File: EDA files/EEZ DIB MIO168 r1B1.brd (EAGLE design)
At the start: 146 x 95 mm, 296 parts, among them IC1 M24C32-WMN6P, IC10 DAC7760IPWPR, IC11 DAC7760IPWPR, IC12 OPA376AIDBVR, IC13 DAC7563TDGSR, IC14 OPA2196IDR, IC15 BTS3408G, IC16 BTS3408G, IC17 BTS3408G, IC18 BTS3408G, IC19 74HC126PW,118, IC2 Si8641BB-B-IS1, IC20 TL431B, IC21 DG468DV-T1-E3, IC22 DG468DV-T1-E3, IC23 DG468DV-T1-E3, IC24 DG468DV-T1-E3, IC25 DG468DV-T1-E3, IC26 DG468DV-T1-E3, IC27 DG468DV-T1-E3, IC28 DG468DV-T1-E3, IC29 DG468DV-T1-E3, IC3 Si8641BB-B-IS1, IC30 DG468DV-T1-E3, IC31 DG468DV-T1-E3, IC32 DG468DV-T1-E3, IC33 DG468DV-T1-E3, IC34 DG468DV-T1-E3, IC35 OPA376AIDBVR, IC36 ADS8674IDBT, IC4 L78L12, IC5 LP2985-50DBVR, IC6 LP2985-33DBVR, IC7 L79L12, IC8 STM32F446ZCT6, IC9 OPA2196IDR, J1 4907, J2 503398-1892, Q1 2N7002PS, Q10 BSS169, Q11 BSS169, Q12 BSS169, Q13 BSS169, Q2 2N7002PS, Q3 2N7002PS, Q4 2N7002PS, Q5 2N7002PS, Q6 BSS169, Q7 BSS169, Q8 BSS169, Q9 BSS169, X1 77317-104-28LF, X2 SSW-106-02-S-S, X3 691327310016, X4 691327310016, Y1 25MHz

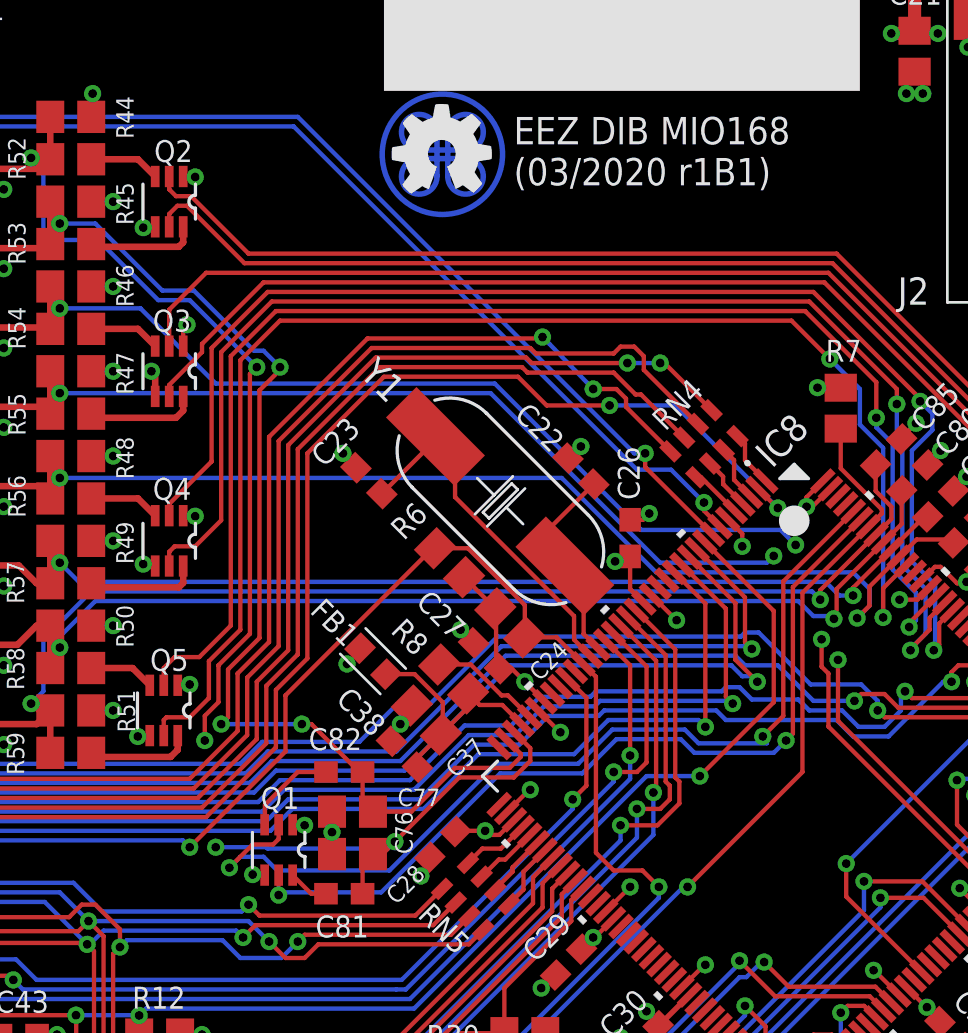
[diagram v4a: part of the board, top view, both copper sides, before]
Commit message: 2N7002PS package fixed
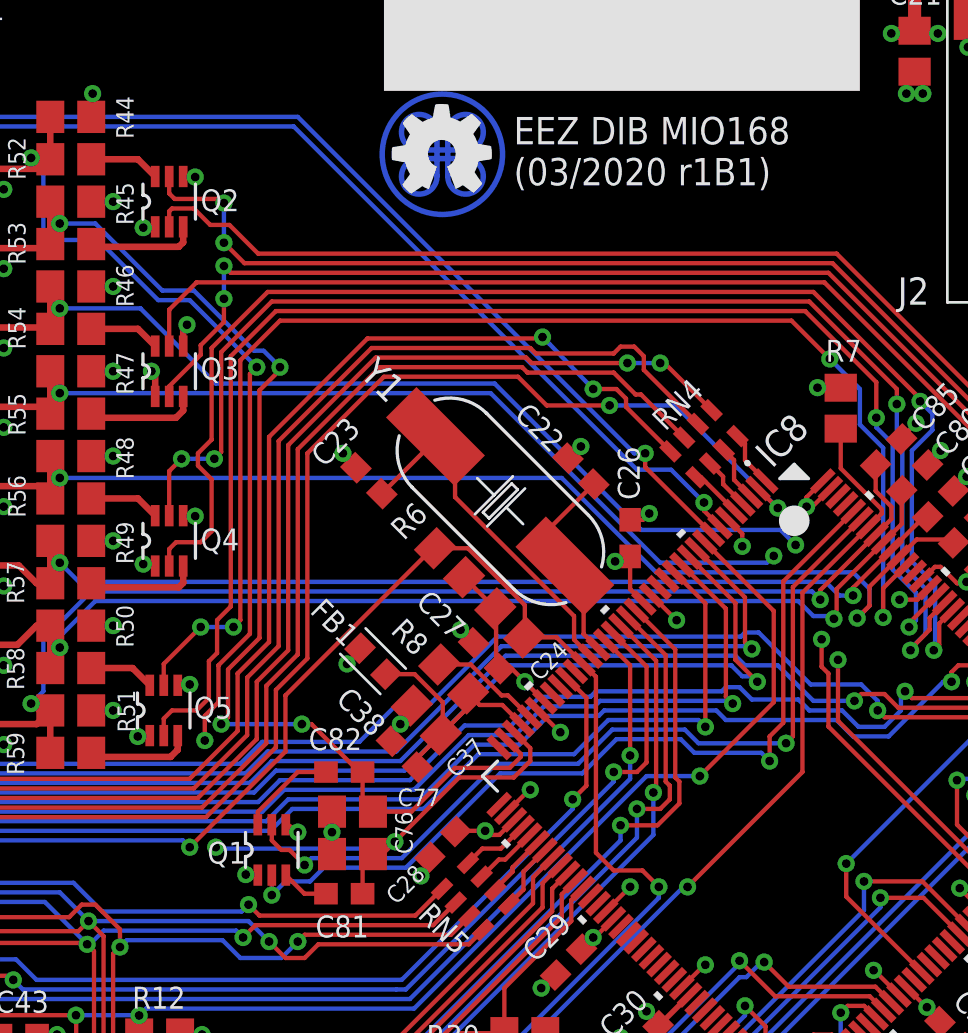
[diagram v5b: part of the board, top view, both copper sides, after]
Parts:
- Q1, Q2, Q3, Q4, Q5: value 2N7002PS -> 2N7002PS,115
- moved Q1 0.32 mm to (97.2, 52.3), turned to 90 degrees
- turned Q2 to 90 degrees
- turned Q3 to 90 degrees
- turned Q4 to 90 degrees
- turned Q5 to 90 degrees
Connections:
- net N$10: now also Q3.6; no longer Q3.3
- net N$13: now also Q3.3; no longer Q3.6
- net N$15: now also Q4.6; no longer Q4.3
- net N$16: now also Q4.3; no longer Q4.6
- net N$17: now also Q5.6; no longer Q5.3
- net N$23: now also Q5.3; no longer Q5.6
- net N$24: now also Q1.3; no longer Q1.6
- net N$76: now also Q1.6; no longer Q1.3
- net N$8: now also Q2.6; no longer Q2.3
- net N$9: now also Q2.3; no longer Q2.6
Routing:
- net SLOW_DIN#1: track 44.6 -> 40.7 mm
- net IN_CTRL4: track 59.6 -> 63.1 mm
- net IN_CTRL6: track 63.7 -> 66.1 mm
- net IN_CTRL2: track 55.2 -> 57.5 mm, vias 0 -> 2
- net IN_CTRL7: track 64.3 -> 62.2 mm, vias 2 -> 4
- net IN_CTRL5: track 61.3 -> 59.3 mm, vias 2 -> 4
- net IN_CTRL1: track 55.7 -> 57.2 mm, vias 0 -> 2
- net IN_CTRL3: track 54.4 -> 53.9 mm

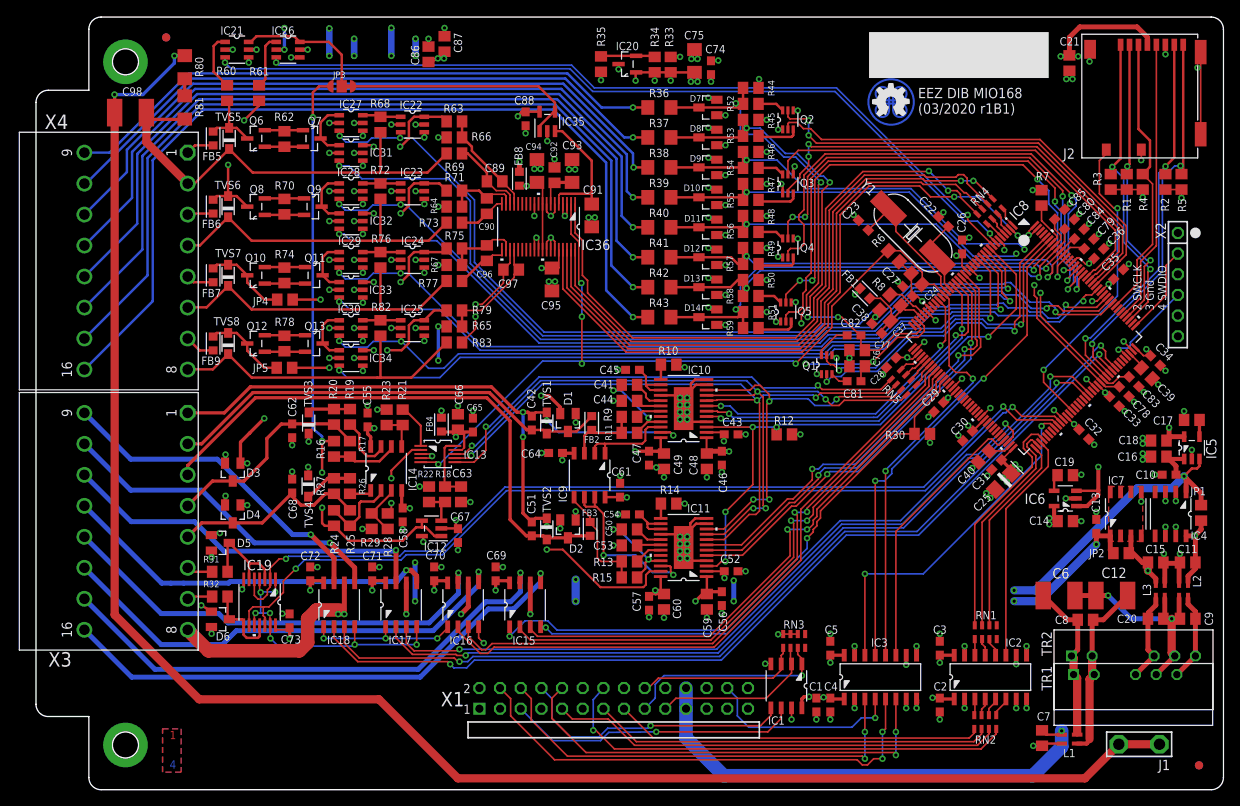
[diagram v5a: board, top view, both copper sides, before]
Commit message: front panel connectors position adjusted
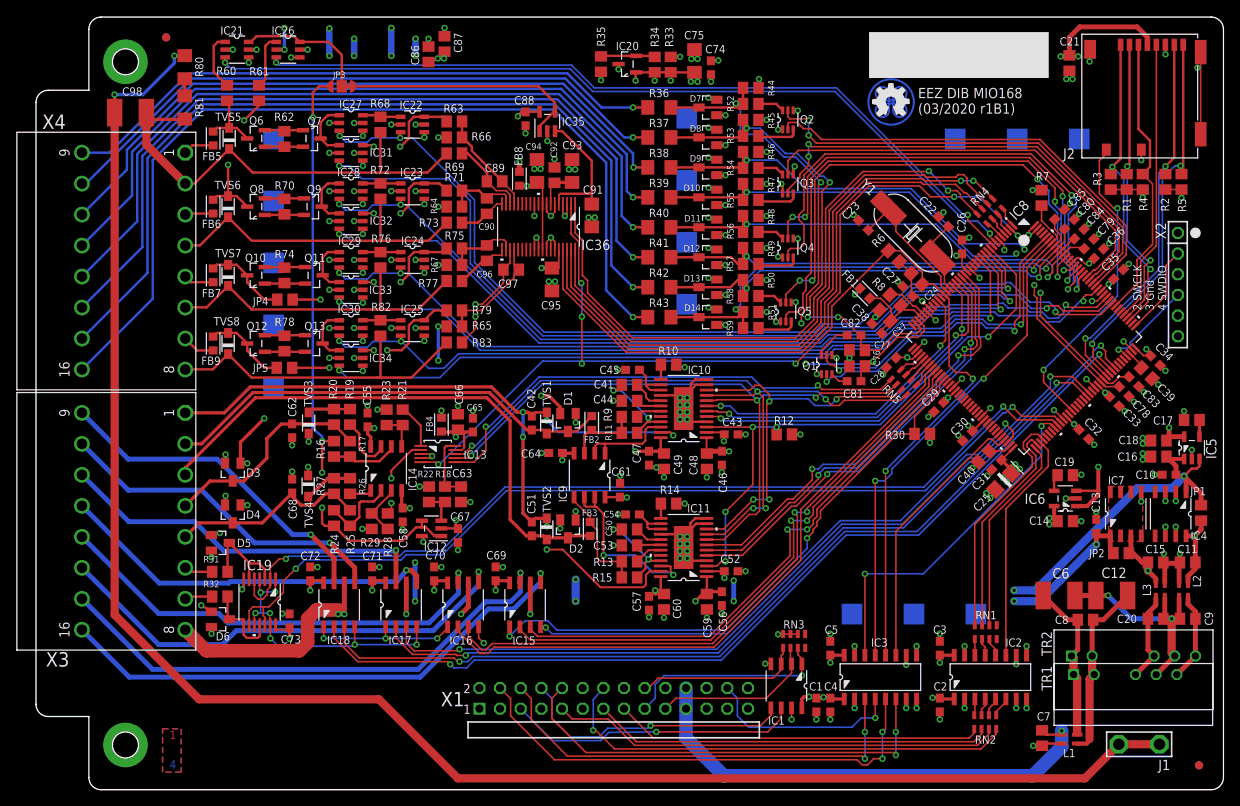
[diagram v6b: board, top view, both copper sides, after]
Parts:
- R31, R32: value 47R -> 100R
- moved X3 0.30 mm to (12.0, 33.0)
- moved X4 0.30 mm to (12.0, 65.0)
- moved SH4 0.25 mm to (18.2, 19.7)
